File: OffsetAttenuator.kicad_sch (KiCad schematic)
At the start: 17 parts, among them J1 Conn_Coaxial, J2 Conn_Coaxial, SW1 POWER, SW2 BYPASS, U1 L7805, X1 4MHz

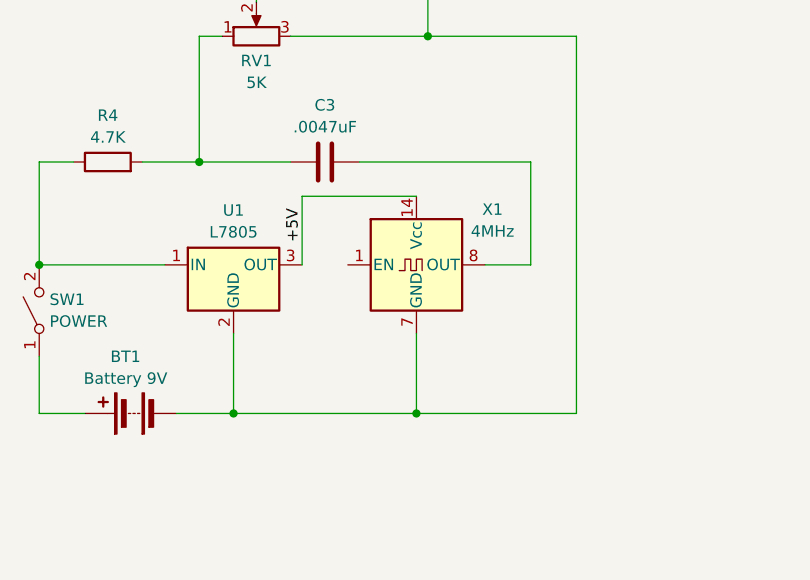
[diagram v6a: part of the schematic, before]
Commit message: adding osc schematic and footprint
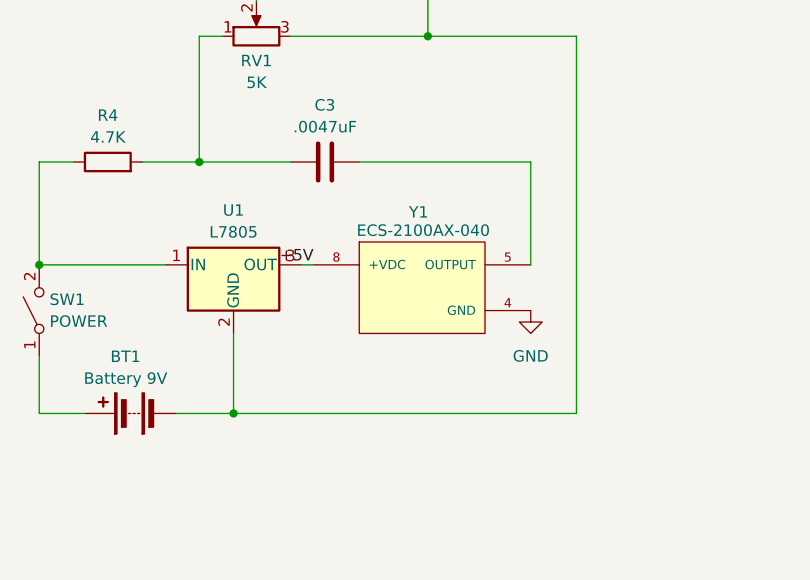
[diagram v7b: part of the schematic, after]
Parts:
- removed X1: 4MHz, Library:OSC_ECS-2100AX-040, symbol Oscillator:CXO_DIP14
- added Y1: ECS-2100AX-040, Library:OSC_ECS-2100AX-040, symbol OSC:ECS-2100AX-040
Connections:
- net +5V: now also Y1.8 (+VDC)
- net GND: now also Y1.4 (GND)
- net at C3.2: now also Y1.5 (OUTPUT)
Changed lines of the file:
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@@
 		(color 0 0 0 0)
 	)
-	(junction
-		(at 151.13 154.94)
-		(diameter 0)
-		(color 0 0 0 0)
-	)
 	(wire
 		(pts
@@
 	(wire
 		(pts
-			(xy 151.13 146.05) (xy 151.13 154.94)
-		)
-		(stroke
-			(width 0)
-			(type default)
-		)
-	)
-	(wire
-		(pts
 			(xy 133.35 95.25) (xy 124.46 95.25)
 		)
@@
 	(wire
 		(pts
+			(xy 163.83 127) (xy 163.83 138.43)
+		)
+		(stroke
+			(width 0)
+			(type default)
+		)
+	)
+	(wire
+		(pts
 			(xy 104.14 95.25) (xy 110.49 95.25)
 		)
@@
 	(wire
 		(pts
+			(xy 138.43 138.43) (xy 139.7 138.43)
+		)
+		(stroke
+			(width 0)
+			(type default)
+		)
+	)
+	(wire
+		(pts
 			(xy 114.3 154.94) (xy 109.22 154.94)
 		)
@@
 	(wire
 		(pts
-			(xy 138.43 130.81) (xy 151.13 130.81)
-		)
-		(stroke
-			(width 0)
-			(type default)
-		)
-	)
-	(wire
-		(pts
 			(xy 152.4 95.25) (xy 163.83 95.25)
 		)
@@
 	(wire
 		(pts
-			(xy 158.75 138.43) (xy 163.83 138.43)
-		)
-		(stroke
-			(width 0)
-			(type default)
-		)
-	)
-	(wire
-		(pts
 			(xy 110.49 95.25) (xy 116.84 95.25)
 		)
@@
 	(wire
 		(pts
-			(xy 151.13 154.94) (xy 130.81 154.94)
-		)
-		(stroke
-			(width 0)
-			(type default)
-		)
-	)
-	(wire
-		(pts
-			(xy 138.43 138.43) (xy 138.43 130.81)
+			(xy 130.81 154.94) (xy 168.91 154.94)
 		)
 		(stroke
@@
 	(wire
 		(pts
-			(xy 163.83 138.43) (xy 163.83 127)
-		)
-		(stroke
-			(width 0)
-			(type default)
-		)
-	)
-	(wire
-		(pts
 			(xy 152.4 95.25) (xy 147.32 95.25)
 		)
@@
 		(pts
 			(xy 109.22 138.43) (xy 123.19 138.43)
-		)
-		(stroke
-			(width 0)
-			(type default)
-		)
-	)
-	(wire
-		(pts
-			(xy 151.13 154.94) (xy 168.91 154.94)
 		)
 		(stroke
@@
 	)
 	(label "+5V"
-		(at 138.43 135.89 90)
+		(at 139.7 138.43 180)
 		(effects
 			(font
 				(size 1.27 1.27)
 			)
-			(justify left bottom)
+			(justify right bottom)
 		)
 	)
@@
 	)
 	(symbol
+		(lib_id "OSC:ECS-2100AX-040")
+		(at 157.48 138.43 0)
+		(unit 1)
+		(exclude_from_sim no)
+		(in_bom yes)
+		(on_board yes)
+		(dnp no)
+		(property "Reference" "Y1"
+			(at 151.384 132.588 0)
+			(effects
+				(font
+					(size 1.27 1.27)
+				)
+			)
+		)
+		(property "Value" "ECS-2100AX-040"
+			(at 151.892 134.62 0)
+			(effects
+				(font
+					(size 1.27 1.27)
+				)
+			)
+		)
+		(property "Footprint" "Library:OSC_ECS-2100AX-040"
+			(at 157.48 138.43 0)
+			(effects
+				(font
+					(size 1.27 1.27)
+				)
+				(justify bottom)
+				(hide yes)
+			)
+		)
+		(property "Datasheet" ""
+			(at 157.48 138.43 0)
+			(effects
+				(font
+					(size 1.27 1.27)
+				)
+				(hide yes)
+			)
+		)
+		(property "Description" ""
+			(at 157.48 138.43 0)
+			(effects
+				(font
+					(size 1.27 1.27)
+				)
+				(hide yes)
+			)
+		)
+		(property "PARTREV" "N/A"
+			(at 157.48 138.43 0)
+			(effects
+				(font
+					(size 1.27 1.27)
+				)
+				(justify bottom)
+				(hide yes)
+			)
+		)
+		(property "STANDARD" "Manufacturer Recommendation"
+			(at 157.48 138.43 0)
+			(effects
+				(font
+					(size 1.27 1.27)
+				)
+				(justify bottom)
+				(hide yes)
+			)
+		)
+		(property "MANUFACTURER" "ECS Inc."
+			(at 157.48 138.43 0)
+			(effects
+				(font
+					(size 1.27 1.27)
+				)
+				(justify bottom)
+				(hide yes)
+			)
+		)
+		(pin "8"
+		)
+		(pin "5"
+		)
+		(pin "4"
+		)
+		(instances
+			(project ""
+				(path "/1ad55a5d-7440-488e-8560-ee9e41fda5dc"
+					(reference "Y1")
+					(unit 1)
+				)
+			)
+		)
+	)
+	(symbol
 		(lib_id "Device:C")
 		(at 167.64 95.25 90)
@@
 				(path "/1ad55a5d-7440-488e-8560-ee9e41fda5dc"
 					(reference "C2")
-					(unit 1)
-				)
-			)
-		)
-	)
-	(symbol
-		(lib_id "Oscillator:CXO_DIP14")
-		(at 151.13 138.43 0)
-		(unit 1)
-		(exclude_from_sim no)
-		(in_bom yes)
-		(on_board yes)
-		(dnp no)
-		(fields_autoplaced yes)
-		(property "Reference" "X1"
-			(at 159.5929 132.285 0)
-			(effects
-				(font
-					(size 1.27 1.27)
-				)
-			)
-		)
-		(property "Value" "4MHz"
-			(at 159.5929 134.7093 0)
-			(effects
-				(font
-					(size 1.27 1.27)
-				)
-			)
-		)
-		(property "Footprint" "Library:OSC_ECS-2100AX-040"
-			(at 162.56 147.32 0)
-			(effects
-				(font
-					(size 1.27 1.27)
-				)
-				(hide yes)
-			)
-		)
-		(property "Datasheet" "http://cdn-reichelt.de/documents/datenblatt/B400/OSZI.pdf"
-			(at 148.59 138.43 0)
-			(effects
-				(font
-					(size 1.27 1.27)
-				)
-				(hide yes)
-			)
-		)
-		(property "Description" "Crystal Clock Oscillator, DIP14-style metal package"
-			(at 151.13 138.43 0)
-			(effects
-				(font
-					(size 1.27 1.27)
-				)
-				(hide yes)
-			)
-		)
-		(pin "1"
-		)
-		(pin "14"
-		)
-		(pin "8"
-		)
-		(pin "7"
-		)
-		(instances
-			(project ""
-				(path "/1ad55a5d-7440-488e-8560-ee9e41fda5dc"
-					(reference "X1")
 					(unit 1)
 				)
@@
 					(unit 1)
 				)
+			)
+		)
+	)
+	(symbol
+		(lib_id "power:GND")
+		(at 163.83 143.51 0)
+		(unit 1)
+		(exclude_from_sim no)
+		(in_bom yes)
+		(on_board yes)
+		(dnp no)
+		(fields_autoplaced yes)
+		(property "Reference" "#PWR04"
+			(at 163.83 149.86 0)
+			(effects
+				(font
+					(size 1.27 1.27)
+				)
+				(hide yes)
+			)
+		)
+		(property "Value" "GND"
+			(at 163.83 148.59 0)
+			(effects
+				(font
+					(size 1.27 1.27)
+				)
+			)
+		)
+		(property "Footprint" ""
+			(at 163.83 143.51 0)
+			(effects
+				(font
+					(size 1.27 1.27)
+				)
+				(hide yes)
+			)
+		)
+		(property "Datasheet" ""
+			(at 163.83 143.51 0)
+			(effects
+				(font
+					(size 1.27 1.27)
+				)
+				(hide yes)
+			)
+		)
+		(property "Description" "Power symbol creates a global label with name \"GND\" , ground"
+			(at 163.83 143.51 0)
+			(effects
+				(font
+					(size 1.27 1.27)
+				)
+				(hide yes)
+			)
+		)
+		(pin "1"
+		)
+		(instances
+			(project ""
+				(path "/1ad55a5d-7440-488e-8560-ee9e41fda5dc"
+					(reference "#PWR04")
+					(unit 1)
+				)

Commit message: pcb layout
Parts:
- BT1: footprint Library:1294PCB_29P57X53P85_KEY -> Connector_PinHeader_2.54mm:PinHeader_1x02_P2.54mm_Vertical
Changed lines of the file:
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@@
 			)
 		)
-		(property "Footprint" "Library:1294PCB_29P57X53P85_KEY"
+		(property "Footprint" "Connector_PinHeader_2.54mm:PinHeader_1x02_P2.54mm_Vertical"
 			(at 117.856 154.94 90)
 			(effects
